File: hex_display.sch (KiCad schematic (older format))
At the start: 24 parts, among them J1 Conn_01x14, J2 Conn_01x14, Q1 MMBT3906, Q2 MMBT3906, Q3 MMBT3906, Q4 MMBT3906, U1 ATMEGA164A-AU, U2 7SEGMENT_CA, U3 7SEGMENT_CA, U4 7SEGMENT_CA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

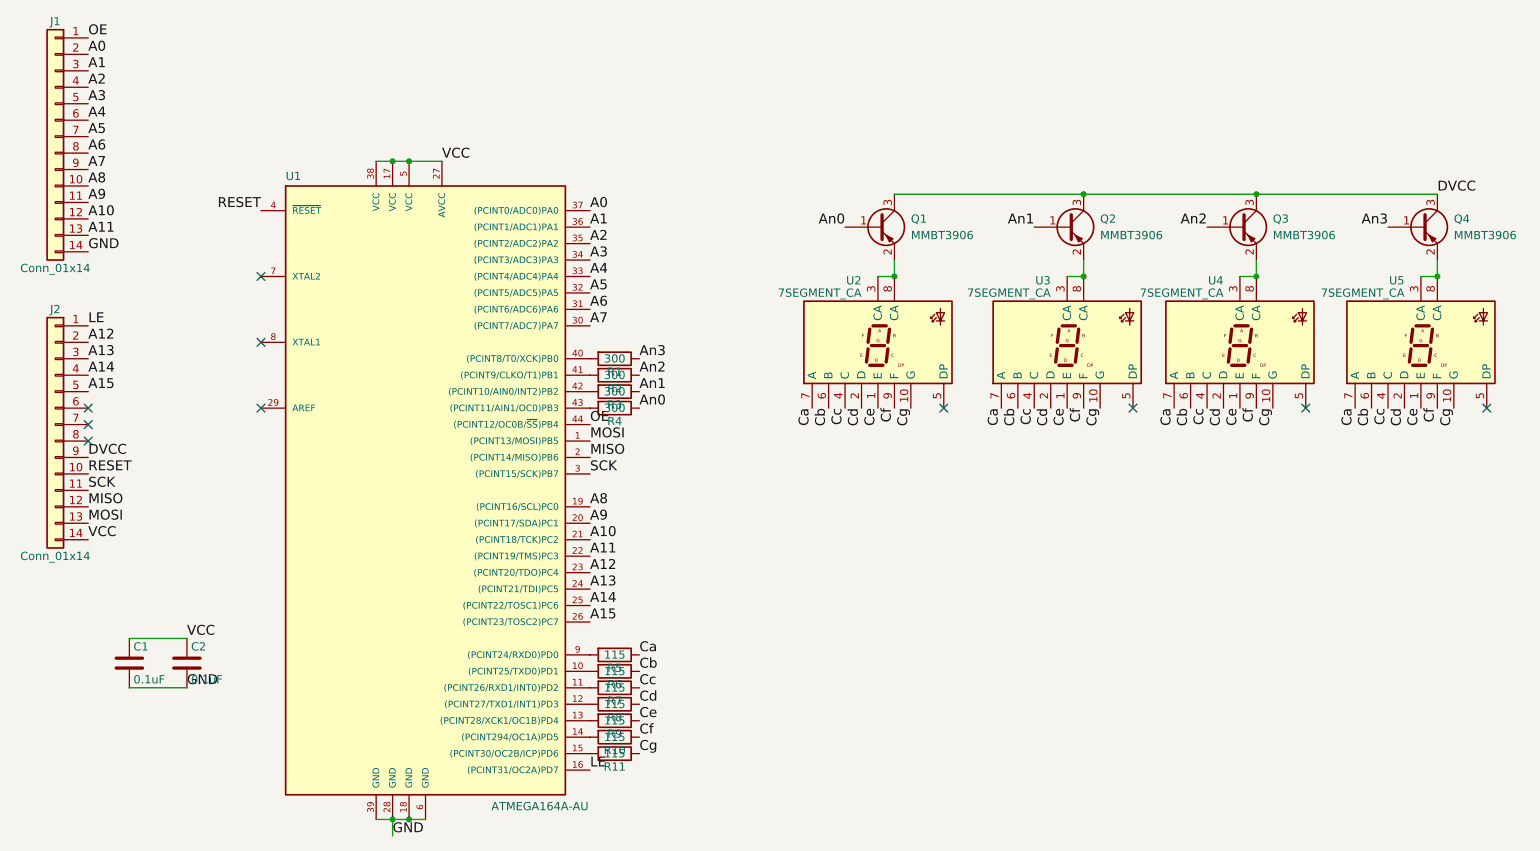
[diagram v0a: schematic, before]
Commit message: assemble the board. change drive resistor to transistor. start a sketch to test the device. having problems being able to program it. not sure if this is the device, or the arduino or the macbook.
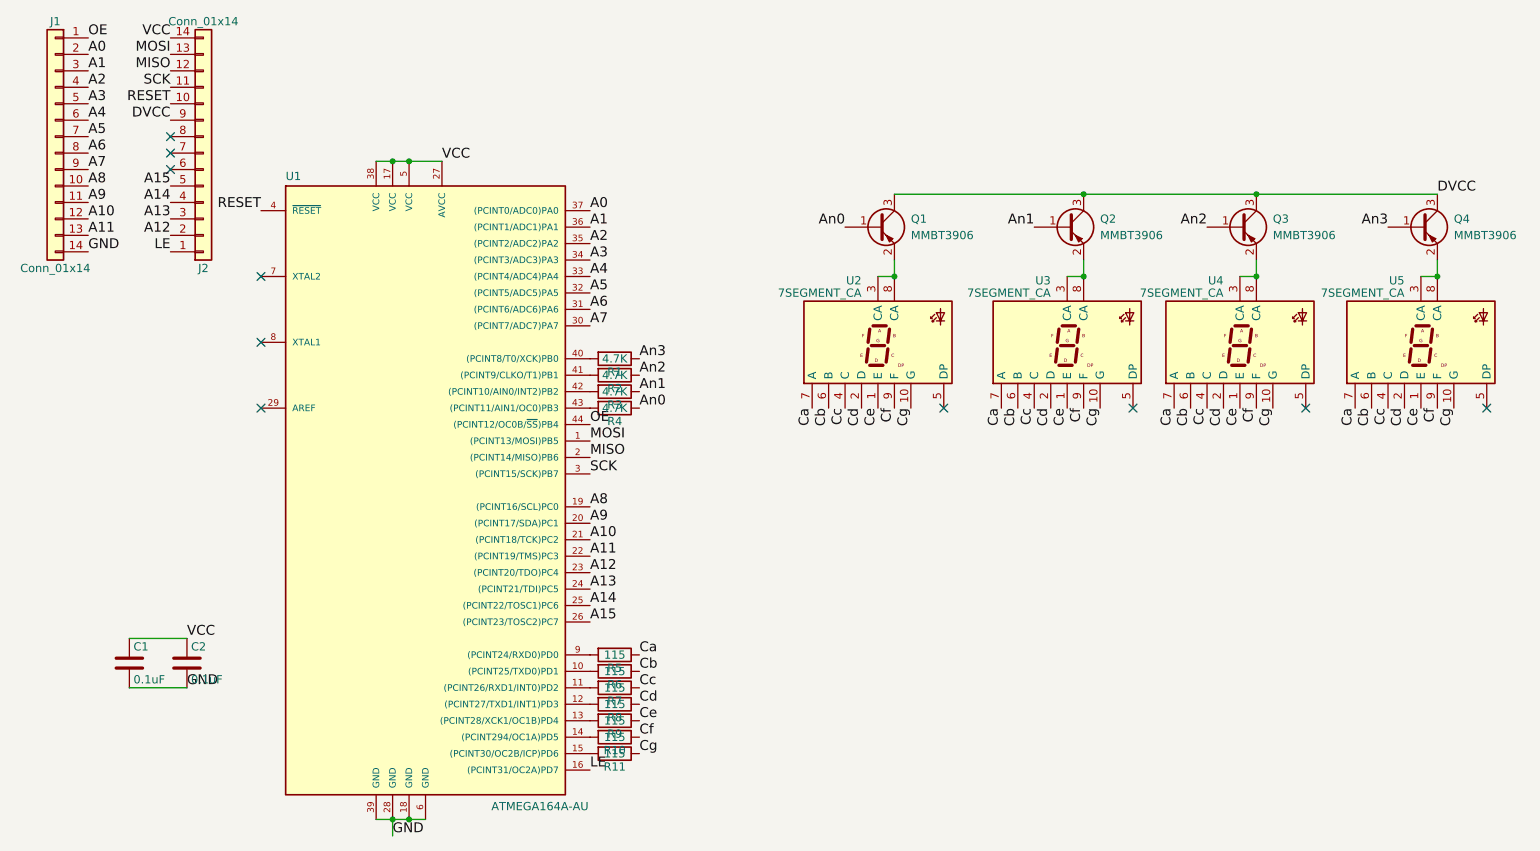
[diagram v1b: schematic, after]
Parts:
- R1, R2, R3, R4: value 300 -> 4.7K
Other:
- moved on the sheet: J2
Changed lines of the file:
@@
 L Conn_01x14 J2
 U 1 1 5A99BB27
-P 800 3200
-F 0 "J2" H 800 3900 50  0000 C CNN
-F 1 "Conn_01x14" H 800 2400 50  0000 C CNN
-F 2 "Pin_Headers:Pin_Header_Straight_1x14_Pitch2.54mm" H 800 3200 50  0001 C CNN
-F 3 "" H 800 3200 50  0001 C CNN
-	1    800  3200
-	-1   0    0    -1
-$EndComp
-Text Label 1000 3900 0    60   ~ 0
+P 1700 1550
+F 0 "J2" H 1700 2250 50  0000 C CNN
+F 1 "Conn_01x14" H 1700 750 50  0000 C CNN
+F 2 "Pin_Headers:Pin_Header_Straight_1x14_Pitch2.54mm" H 1700 1550 50  0001 C CNN
+F 3 "" H 1700 1550 50  0001 C CNN
+	1    1700 1550
+	1    0    0    1
+$EndComp
+Text Label 1500 850  2    60   ~ 0
 VCC
 Text Label 1000 2150 0    60   ~ 0
@@
 Text Label 1000 850  0    60   ~ 0
 OE
-Text Label 1000 2600 0    60   ~ 0
+Text Label 1500 2150 2    60   ~ 0
 LE
 Text Label 1000 950  0    60   ~ 0
@@
 Text Label 1000 2050 0    60   ~ 0
 A11
-Text Label 1000 2700 0    60   ~ 0
+Text Label 1500 2050 2    60   ~ 0
 A12
-Text Label 1000 2800 0    60   ~ 0
+Text Label 1500 1950 2    60   ~ 0
 A13
-Text Label 1000 2900 0    60   ~ 0
+Text Label 1500 1850 2    60   ~ 0
 A14
-Text Label 1000 3000 0    60   ~ 0
+Text Label 1500 1750 2    60   ~ 0
 A15
-Text Label 1000 3800 0    60   ~ 0
+Text Label 1500 950  2    60   ~ 0
 MOSI
-Text Label 1000 3700 0    60   ~ 0
+Text Label 1500 1050 2    60   ~ 0
 MISO
-Text Label 1000 3600 0    60   ~ 0
+Text Label 1500 1150 2    60   ~ 0
 SCK
-Text Label 1000 3500 0    60   ~ 0
+Text Label 1500 1250 2    60   ~ 0
 RESET
 Text Label 4050 3300 0    60   ~ 0
@@
 P 4200 2800
 F 0 "R1" V 4280 2800 50  0000 C CNN
-F 1 "300" V 4200 2800 50  0000 C CNN
+F 1 "4.7K" V 4200 2800 50  0000 C CNN
 F 2 "Resistors_SMD:R_0603" V 4130 2800 50  0001 C CNN
 F 3 "" H 4200 2800 50  0001 C CNN
@@
 P 4200 2900
 F 0 "R2" V 4280 2900 50  0000 C CNN
-F 1 "300" V 4200 2900 50  0000 C CNN
+F 1 "4.7K" V 4200 2900 50  0000 C CNN
 F 2 "Resistors_SMD:R_0603" V 4130 2900 50  0001 C CNN
 F 3 "" H 4200 2900 50  0001 C CNN
@@
 P 4200 3000
 F 0 "R3" V 4280 3000 50  0000 C CNN
-F 1 "300" V 4200 3000 50  0000 C CNN
+F 1 "4.7K" V 4200 3000 50  0000 C CNN
 F 2 "Resistors_SMD:R_0603" V 4130 3000 50  0001 C CNN
 F 3 "" H 4200 3000 50  0001 C CNN
@@
 P 4200 3100
 F 0 "R4" V 4280 3100 50  0000 C CNN
-F 1 "300" V 4200 3100 50  0000 C CNN
+F 1 "4.7K" V 4200 3100 50  0000 C CNN
 F 2 "Resistors_SMD:R_0603" V 4130 3100 50  0001 C CNN
 F 3 "" H 4200 3100 50  0001 C CNN
@@
 NoConn ~ 2050 2700
 NoConn ~ 2050 3100
-NoConn ~ 1000 3200
-NoConn ~ 1000 3300
-NoConn ~ 1000 3100
+NoConn ~ 1500 1550
+NoConn ~ 1500 1450
+NoConn ~ 1500 1650
 Text Label 4050 5300 0    60   ~ 0
 LE
@@
 NoConn ~ 8400 3100
 NoConn ~ 9500 3100
-Text Label 1000 3400 0    60   ~ 0
+Text Label 1500 1350 2    60   ~ 0
 DVCC
 Connection ~ 2950 5600
@@
 Connection ~ 9200 2300
 Wire Wire Line
-	2750 5600 3050 5600
-Wire Wire Line
-	2750 1600 3150 1600
+	2750 5600 2850 5600
+Wire Wire Line
+	2850 5600 2950 5600
+Wire Wire Line
+	2950 5600 3050 5600
+Wire Wire Line
+	2750 1600 2850 1600
+Wire Wire Line
+	2850 1600 2950 1600
+Wire Wire Line
+	2950 1600 3150 1600
 Connection ~ 2850 1600
 Wire Wire Line
-	5900 1800 9200 1800
+	5900 1800 7050 1800
+Wire Wire Line
+	7050 1800 8100 1800
+Wire Wire Line
+	8100 1800 9200 1800
 Connection ~ 7050 1800
 Connection ~ 8100 1800

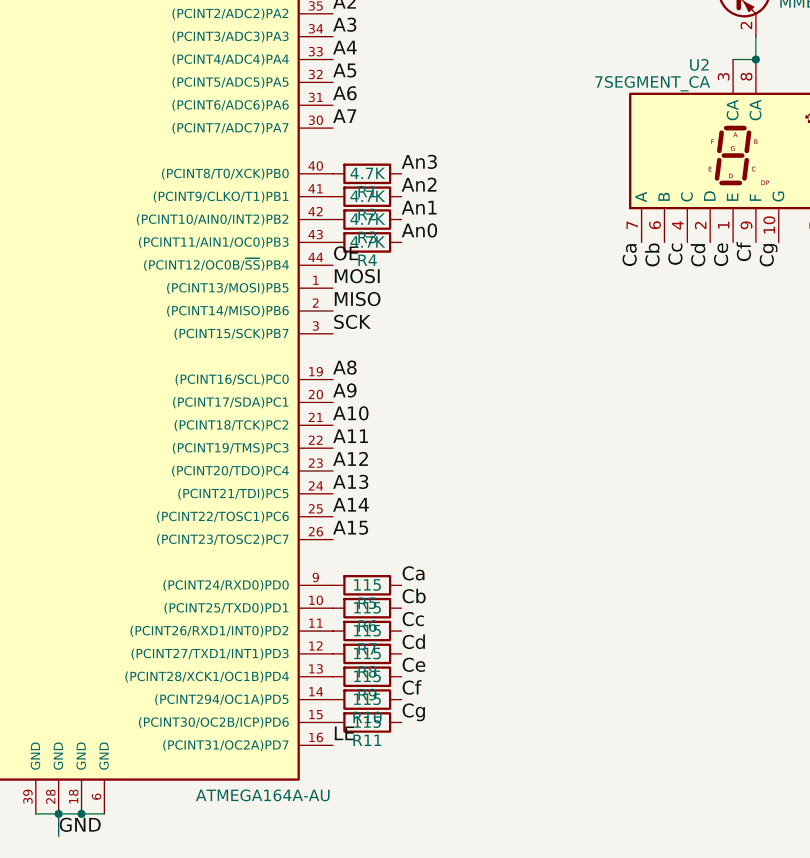
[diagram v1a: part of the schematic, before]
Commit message: change out resistor values
during testing, noticed the displays seemed kind of dim. Experimented with values I had handy until it looked good.
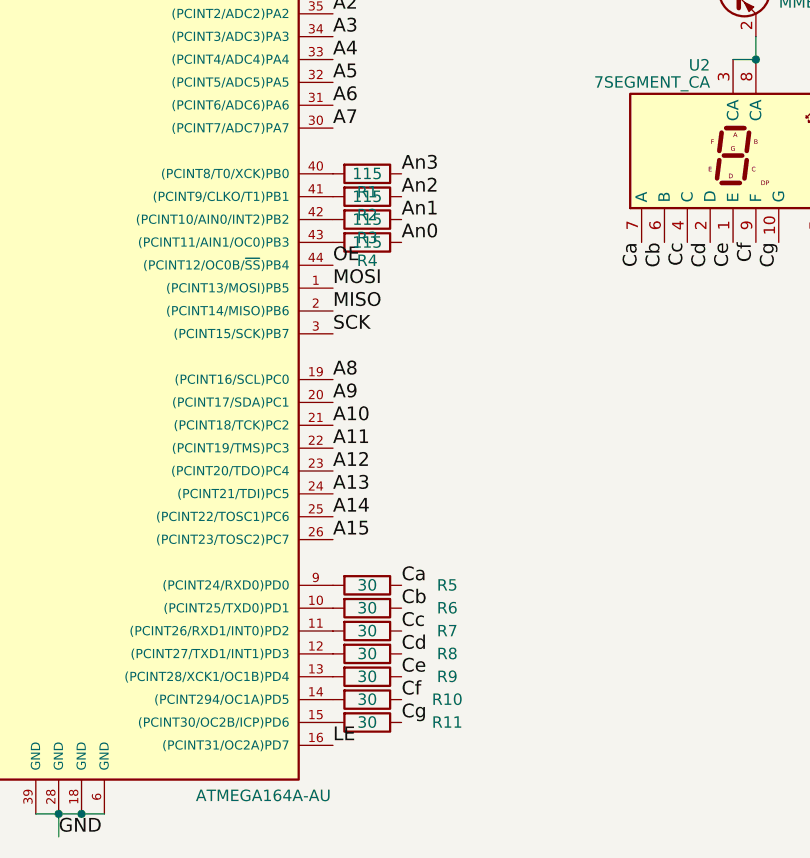
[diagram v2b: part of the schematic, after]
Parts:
- R1, R2, R3, R4: value 4.7K -> 115
- R10, R11, R5, R6, R7, R8, R9: value 115 -> 30
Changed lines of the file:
@@
 P 4200 2800
 F 0 "R1" V 4280 2800 50  0000 C CNN
-F 1 "4.7K" V 4200 2800 50  0000 C CNN
+F 1 "115" V 4200 2800 50  0000 C CNN
 F 2 "Resistors_SMD:R_0603" V 4130 2800 50  0001 C CNN
 F 3 "" H 4200 2800 50  0001 C CNN
@@
 P 4200 2900
 F 0 "R2" V 4280 2900 50  0000 C CNN
-F 1 "4.7K" V 4200 2900 50  0000 C CNN
+F 1 "115" V 4200 2900 50  0000 C CNN
 F 2 "Resistors_SMD:R_0603" V 4130 2900 50  0001 C CNN
 F 3 "" H 4200 2900 50  0001 C CNN
@@
 P 4200 3000
 F 0 "R3" V 4280 3000 50  0000 C CNN
-F 1 "4.7K" V 4200 3000 50  0000 C CNN
+F 1 "115" V 4200 3000 50  0000 C CNN
 F 2 "Resistors_SMD:R_0603" V 4130 3000 50  0001 C CNN
 F 3 "" H 4200 3000 50  0001 C CNN
@@
 P 4200 3100
 F 0 "R4" V 4280 3100 50  0000 C CNN
-F 1 "4.7K" V 4200 3100 50  0000 C CNN
+F 1 "115" V 4200 3100 50  0000 C CNN
 F 2 "Resistors_SMD:R_0603" V 4130 3100 50  0001 C CNN
 F 3 "" H 4200 3100 50  0001 C CNN
@@
 U 1 1 5A9AE546
 P 4200 4600
-F 0 "R5" V 4280 4600 50  0000 C CNN
-F 1 "115" V 4200 4600 50  0000 C CNN
+F 0 "R5" V 4200 4950 50  0000 C CNN
+F 1 "30" V 4200 4600 50  0000 C CNN
 F 2 "Resistors_SMD:R_0603" V 4130 4600 50  0001 C CNN
 F 3 "" H 4200 4600 50  0001 C CNN
@@
 U 1 1 5A9AE5B5
 P 4200 4700
-F 0 "R6" V 4280 4700 50  0000 C CNN
-F 1 "115" V 4200 4700 50  0000 C CNN
+F 0 "R6" V 4200 5050 50  0000 C CNN
+F 1 "30" V 4200 4700 50  0000 C CNN
 F 2 "Resistors_SMD:R_0603" V 4130 4700 50  0001 C CNN
 F 3 "" H 4200 4700 50  0001 C CNN
@@
 U 1 1 5A9AE5F1
 P 4200 4800
-F 0 "R7" V 4280 4800 50  0000 C CNN
-F 1 "115" V 4200 4800 50  0000 C CNN
+F 0 "R7" V 4200 5150 50  0000 C CNN
+F 1 "30" V 4200 4800 50  0000 C CNN
 F 2 "Resistors_SMD:R_0603" V 4130 4800 50  0001 C CNN
 F 3 "" H 4200 4800 50  0001 C CNN
@@
 U 1 1 5A9AE5F7
 P 4200 4900
-F 0 "R8" V 4280 4900 50  0000 C CNN
-F 1 "115" V 4200 4900 50  0000 C CNN
+F 0 "R8" V 4200 5250 50  0000 C CNN
+F 1 "30" V 4200 4900 50  0000 C CNN
 F 2 "Resistors_SMD:R_0603" V 4130 4900 50  0001 C CNN
 F 3 "" H 4200 4900 50  0001 C CNN
@@
 U 1 1 5A9AE687
 P 4200 5000
-F 0 "R9" V 4280 5000 50  0000 C CNN
-F 1 "115" V 4200 5000 50  0000 C CNN
+F 0 "R9" V 4200 5350 50  0000 C CNN
+F 1 "30" V 4200 5000 50  0000 C CNN
 F 2 "Resistors_SMD:R_0603" V 4130 5000 50  0001 C CNN
 F 3 "" H 4200 5000 50  0001 C CNN
@@
 U 1 1 5A9AE68D
 P 4200 5100
-F 0 "R10" V 4280 5100 50  0000 C CNN
-F 1 "115" V 4200 5100 50  0000 C CNN
+F 0 "R10" V 4200 5450 50  0000 C CNN
+F 1 "30" V 4200 5100 50  0000 C CNN
 F 2 "Resistors_SMD:R_0603" V 4130 5100 50  0001 C CNN
 F 3 "" H 4200 5100 50  0001 C CNN
@@
 U 1 1 5A9AE693
 P 4200 5200
-F 0 "R11" V 4280 5200 50  0000 C CNN
-F 1 "115" V 4200 5200 50  0000 C CNN
+F 0 "R11" V 4200 5550 50  0000 C CNN
+F 1 "30" V 4200 5200 50  0000 C CNN
 F 2 "Resistors_SMD:R_0603" V 4130 5200 50  0001 C CNN
 F 3 "" H 4200 5200 50  0001 C CNN
